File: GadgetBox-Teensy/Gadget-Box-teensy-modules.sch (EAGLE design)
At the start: 13 parts, among them U3 TEENSY_3.1_ALL_PINS

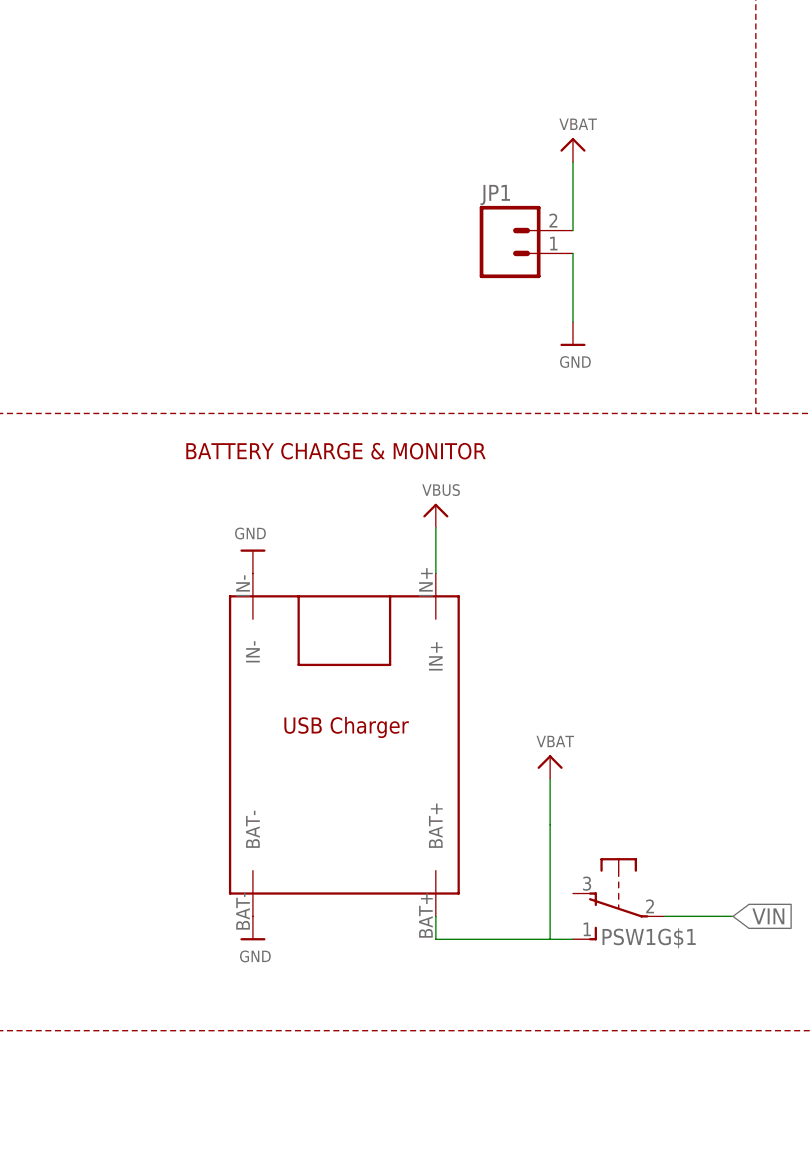
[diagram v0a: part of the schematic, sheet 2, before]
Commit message: Fixed charging circuit
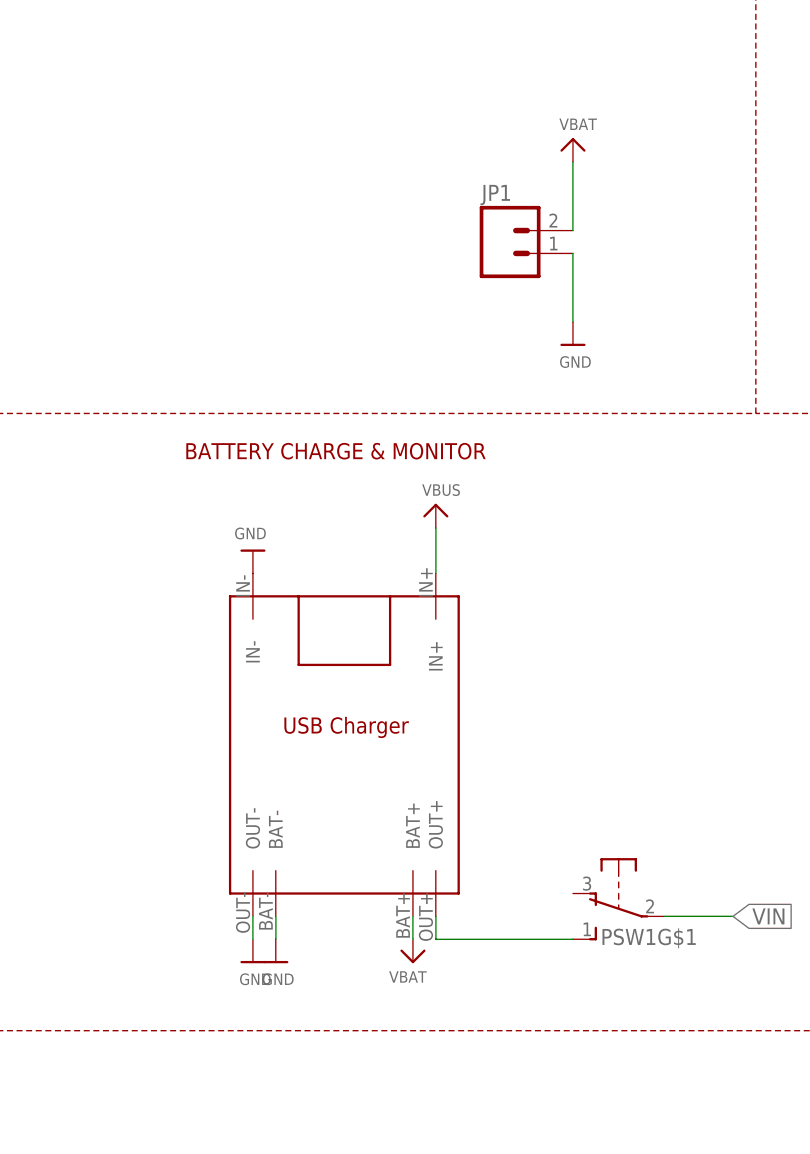
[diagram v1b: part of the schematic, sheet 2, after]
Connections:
- removed net VBATTERY: JP1.2, PSW1G$1.S, R5A.2, U$1.BAT+
- new net VBAT: U3.VBAT
- new net VBATTTERY: JP1.2, R5A.2, U$1.BAT+
- new net VOUT: PSW1G$1.S, U$1.OUT+
- net GND: now also U$1.OUT-
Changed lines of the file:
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@@
 <part name="3V3_PWR9" library="GadgetFactory" deviceset="3V3" device=""/>
 <part name="FRAME2" library="microbuilder" deviceset="FRAME_A4" device=""/>
-<part name="U$21" library="microbuilder" deviceset="VBAT" device=""/>
 <part name="U$16" library="microbuilder" deviceset="VBAT" device=""/>
 <part name="U$22" library="microbuilder" deviceset="GND" device=""/>
@@
 <part name="U$9" library="microbuilder" deviceset="VBAT" device=""/>
 <part name="U$10" library="microbuilder" deviceset="GND" device=""/>
-<part name="U$11" library="microbuilder" deviceset="GND" device=""/>
 <part name="5V0_PWR2" library="GadgetFactory" deviceset="5V0" device=""/>
 <part name="5V0_PWR3" library="GadgetFactory" deviceset="5V0" device=""/>
@@
 <part name="U$2" library="microbuilder" deviceset="VBUS" device=""/>
 <part name="U$3" library="microbuilder" deviceset="GND" device=""/>
+<part name="U$4" library="microbuilder" deviceset="GND" device=""/>
+<part name="U$5" library="microbuilder" deviceset="GND" device=""/>
+<part name="U$6" library="microbuilder" deviceset="VBAT" device=""/>
 </parts>
 <sheets>
@@
 </segment>
 </net>
+<net name="VBAT" class="0">
+<segment>
+<pinref part="U3" gate="G$1" pin="VBAT"/>
+<wire x1="226.06" y1="149.86" x2="228.6" y2="149.86" width="0.2032" layer="91"/>
+</segment>
+</net>
 </nets>
 </sheet>
@@
 <instances>
 <instance part="FRAME2" gate="G$3" x="134.62" y="2.54"/>
-<instance part="U$21" gate="G$1" x="88.9" y="83.82"/>
 <instance part="U$16" gate="G$1" x="91.44" y="152.4"/>
 <instance part="U$22" gate="G$1" x="91.44" y="129.54"/>
@@
 <instance part="U$9" gate="G$1" x="170.18" y="111.76"/>
 <instance part="U$10" gate="G$1" x="170.18" y="76.2"/>
-<instance part="U$11" gate="G$1" x="55.88" y="63.5"/>
 <instance part="JP1" gate="G$1" x="83.82" y="139.7">
 <attribute name="PARTNO" x="83.82" y="139.7" size="1.778" layer="96" display="off"/>
@@
 <instance part="U$2" gate="G$1" x="76.2" y="111.76"/>
 <instance part="U$3" gate="G$1" x="55.88" y="106.68" rot="R180"/>
+<instance part="U$4" gate="G$1" x="55.88" y="60.96"/>
+<instance part="U$5" gate="G$1" x="58.42" y="60.96"/>
+<instance part="U$6" gate="G$1" x="73.66" y="60.96" rot="R180"/>
 </instances>
 <busses>
@@
 </segment>
 <segment>
-<pinref part="U$1" gate="G$1" pin="BAT-"/>
-<pinref part="U$11" gate="G$1" pin="GND"/>
-</segment>
-<segment>
 <pinref part="U$1" gate="G$1" pin="IN-"/>
 <pinref part="U$3" gate="G$1" pin="GND"/>
+</segment>
+<segment>
+<pinref part="U$1" gate="G$1" pin="OUT-"/>
+<pinref part="U$4" gate="G$1" pin="GND"/>
+<wire x1="55.88" y1="63.5" x2="55.88" y2="66.04" width="0.1524" layer="91"/>
+</segment>
+<segment>
+<pinref part="U$1" gate="G$1" pin="BAT-"/>
+<pinref part="U$5" gate="G$1" pin="GND"/>
+<wire x1="58.42" y1="63.5" x2="58.42" y2="66.04" width="0.1524" layer="91"/>
 </segment>
 </net>
@@
 <pinref part="U$2" gate="G$1" pin="VBUS"/>
 <wire x1="76.2" y1="104.14" x2="76.2" y2="109.22" width="0.1524" layer="91"/>
-</segment>
-</net>
-<net name="VBATTERY" class="0">
-<segment>
-<pinref part="U$21" gate="G$1" pin="VBAT"/>
-<wire x1="88.9" y1="76.2" x2="88.9" y2="81.28" width="0.1524" layer="91"/>
-<wire x1="88.9" y1="76.2" x2="88.9" y2="63.5" width="0.2032" layer="91"/>
-<pinref part="PSW1" gate="G$1" pin="S"/>
-<wire x1="88.9" y1="63.5" x2="91.44" y2="63.5" width="0.2032" layer="91"/>
-<pinref part="U$1" gate="G$1" pin="BAT+"/>
-<wire x1="76.2" y1="66.04" x2="76.2" y2="63.5" width="0.2032" layer="91"/>
-<wire x1="76.2" y1="63.5" x2="88.9" y2="63.5" width="0.2032" layer="91"/>
-</segment>
-<segment>
-<pinref part="U$16" gate="G$1" pin="VBAT"/>
-<wire x1="91.44" y1="149.86" x2="91.44" y2="142.24" width="0.1524" layer="91"/>
-<pinref part="JP1" gate="G$1" pin="2"/>
-</segment>
-<segment>
-<pinref part="R5" gate="A" pin="2"/>
-<pinref part="U$9" gate="G$1" pin="VBAT"/>
-<wire x1="170.18" y1="109.22" x2="170.18" y2="106.68" width="0.1524" layer="91"/>
 </segment>
 </net>
@@
 </segment>
 </net>
+<net name="VOUT" class="0">
+<segment>
+<pinref part="PSW1" gate="G$1" pin="S"/>
+<wire x1="76.2" y1="63.5" x2="91.44" y2="63.5" width="0.2032" layer="91"/>
+<pinref part="U$1" gate="G$1" pin="OUT+"/>
+<wire x1="76.2" y1="63.5" x2="76.2" y2="66.04" width="0.2032" layer="91"/>
+</segment>
+</net>
+<net name="VBATTTERY" class="0">
+<segment>
+<pinref part="U$6" gate="G$1" pin="VBAT"/>
+<pinref part="U$1" gate="G$1" pin="BAT+"/>
+<wire x1="73.66" y1="63.5" x2="73.66" y2="66.04" width="0.2032" layer="91"/>
+</segment>
+<segment>
+<pinref part="U$9" gate="G$1" pin="VBAT"/>
+<pinref part="R5" gate="A" pin="2"/>
+<wire x1="170.18" y1="109.22" x2="170.18" y2="106.68" width="0.2032" layer="91"/>
+</segment>
+<segment>
+<pinref part="JP1" gate="G$1" pin="2"/>
+<pinref part="U$16" gate="G$1" pin="VBAT"/>
+<wire x1="91.44" y1="142.24" x2="91.44" y2="149.86" width="0.2032" layer="91"/>
+</segment>
+</net>

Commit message: Fixed Silkscreen
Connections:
- removed net RESET: AH.RESET@1, AL.RESET@1, BH.RESET@1, BL.RESET@1
- net VUSB: now also AH.5V@B7, AL.5V@B7, BH.5V@B7, BL.5V@B7; no longer AH.5V@0, AL.5V@0, BH.5V@0, BL.5V@0
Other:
- moved on the sheet: R4
